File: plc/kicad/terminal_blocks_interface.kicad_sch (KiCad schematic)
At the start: 78 parts, among them CN1 DB128V-5.08-2P-GN-S, CN10 DB128V-5.08-6P-GN-S, CN2 DB128V-5.08-2P-GN-S, CN3 DB128V-5.08-2P-GN-S, CN4 DB128V-5.08-2P-GN-S, CN5 DB128V-5.08-2P-GN-S, CN6 DB128V-5.08-2P-GN-S, CN7 DB128V-5.08-2P-GN-S, CN8 DB128V-5.08-2P-GN-S, CN9 DB128V-5.08-2P-GN-S, Q1 AO3400A, Q2 AO3400A, U1 TCA9535PWR, U2 TPS272C45DRHFR, U3 TPS272C45DRHFR, U4 ADS1115IDGSR, U5 LTV-814S-TA1-A, U6 LTV-814S-TA1-A, U7 LTV-814S-TA1-A, U8 LTV-814S-TA1-A

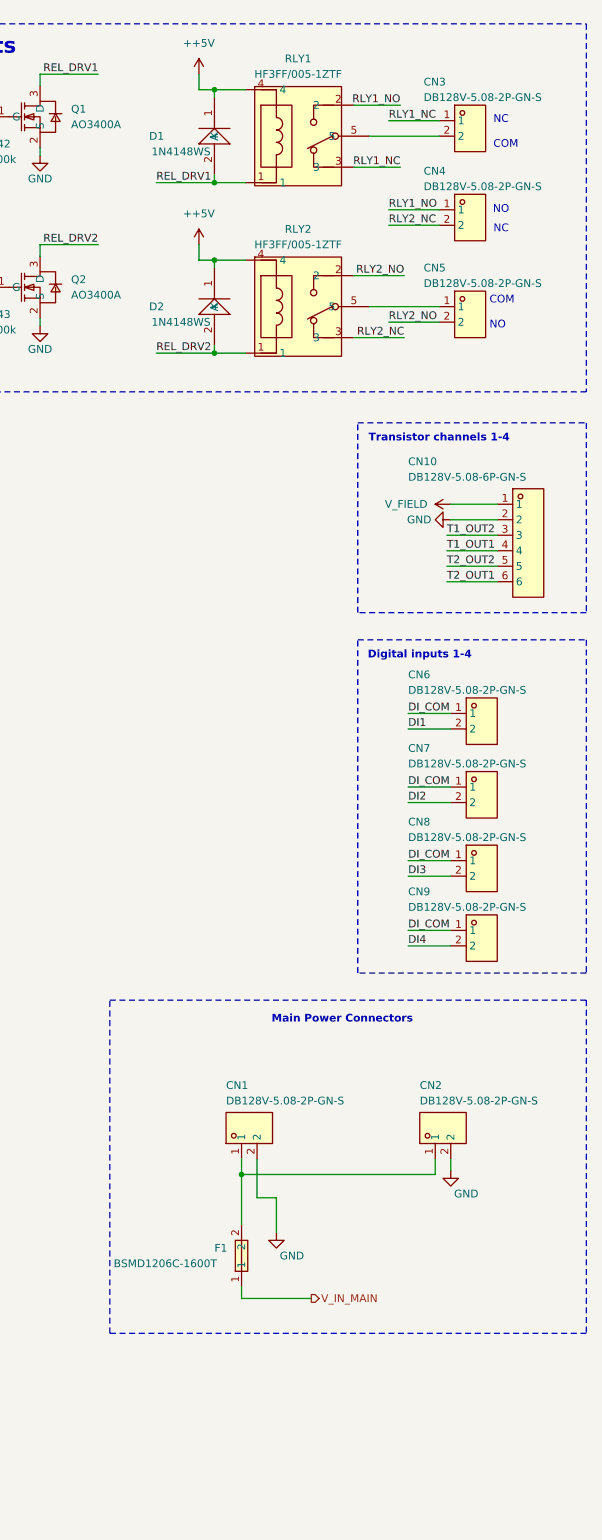
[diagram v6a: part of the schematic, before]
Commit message: Updated PCB placement
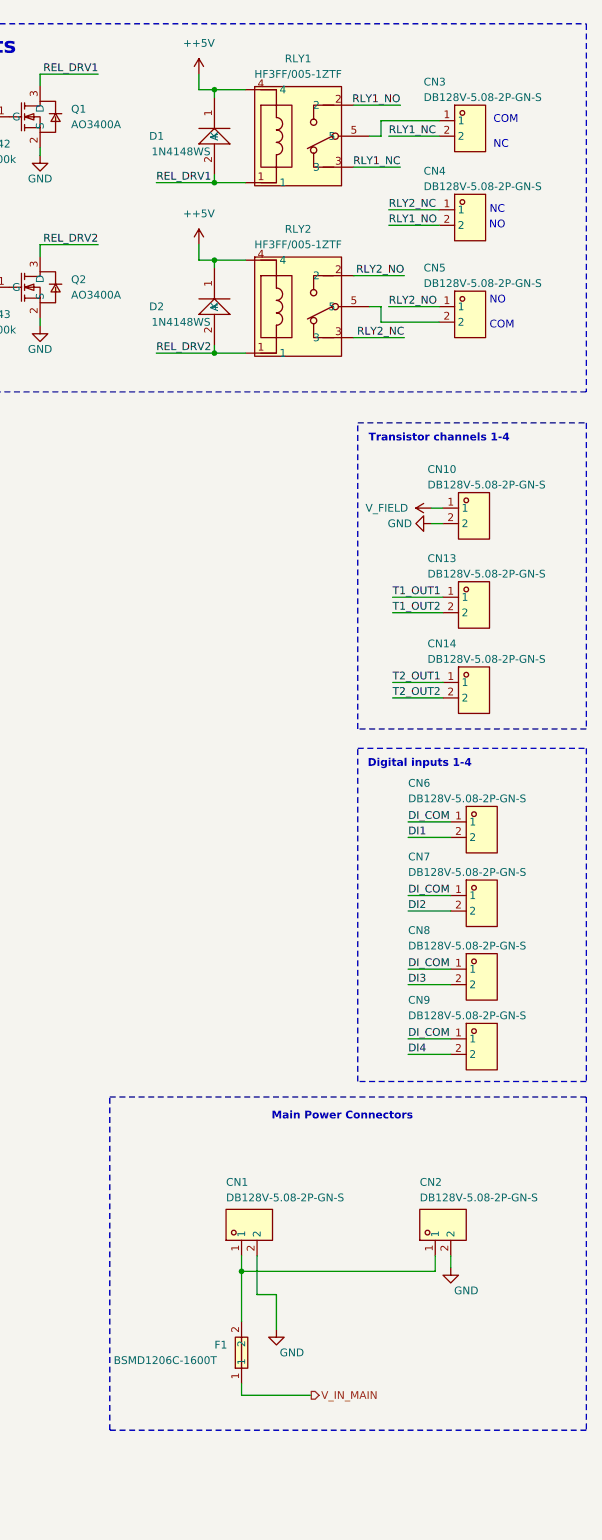
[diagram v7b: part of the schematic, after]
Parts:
- removed CN10: DB128V-5.08-6P-GN-S, LibrePLC32:CONN-TH_6P-P5.08_DIBO_DB128V-5.08, symbol LibrePLC32:DB128V-5.08-6P-GN-S
- added CN10, CN13, CN14: DB128V-5.08-2P-GN-S, LibrePLC32:CONN-TH_2P-P5.08_DIBO_DB128V-5.08, symbol LibrePLC32:DB128V-5.08-2P-GN-S
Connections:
- net GND: now also CN10.2
- net RLY1_NC: now also CN3.2; no longer CN3.1
- net RLY1_NO: now also CN4.2; no longer CN4.1
- net RLY2_NC: now also CN4.1; no longer CN4.2
- net RLY2_NO: now also CN5.1; no longer CN5.2
- net T1_OUT1: now also CN13.1
- net T1_OUT2: now also CN13.2
- net T2_OUT1: now also CN14.1
- net T2_OUT2: now also CN14.2
- net V_FIELD: now also CN10.1
- net at RLY1.5: now also CN3.1; no longer CN3.2
- net at RLY2.5: now also CN5.2; no longer CN5.1
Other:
- note added: "COM NC"
- note added: "NO COM"
- note removed: "COM NO"
- note removed: "NC COM"
- moved on the sheet: CN1, CN2, CN6, CN7, CN8, CN9, F1

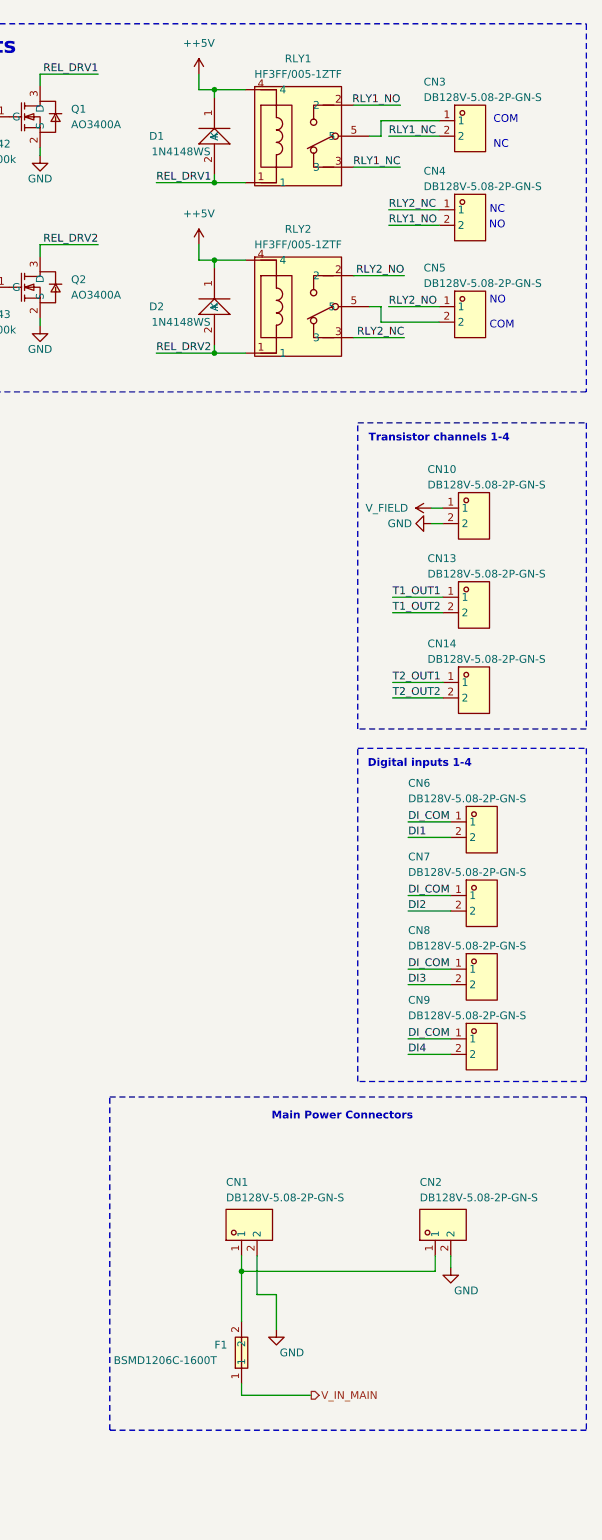
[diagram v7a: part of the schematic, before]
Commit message: Added mounting holes & PCB outline
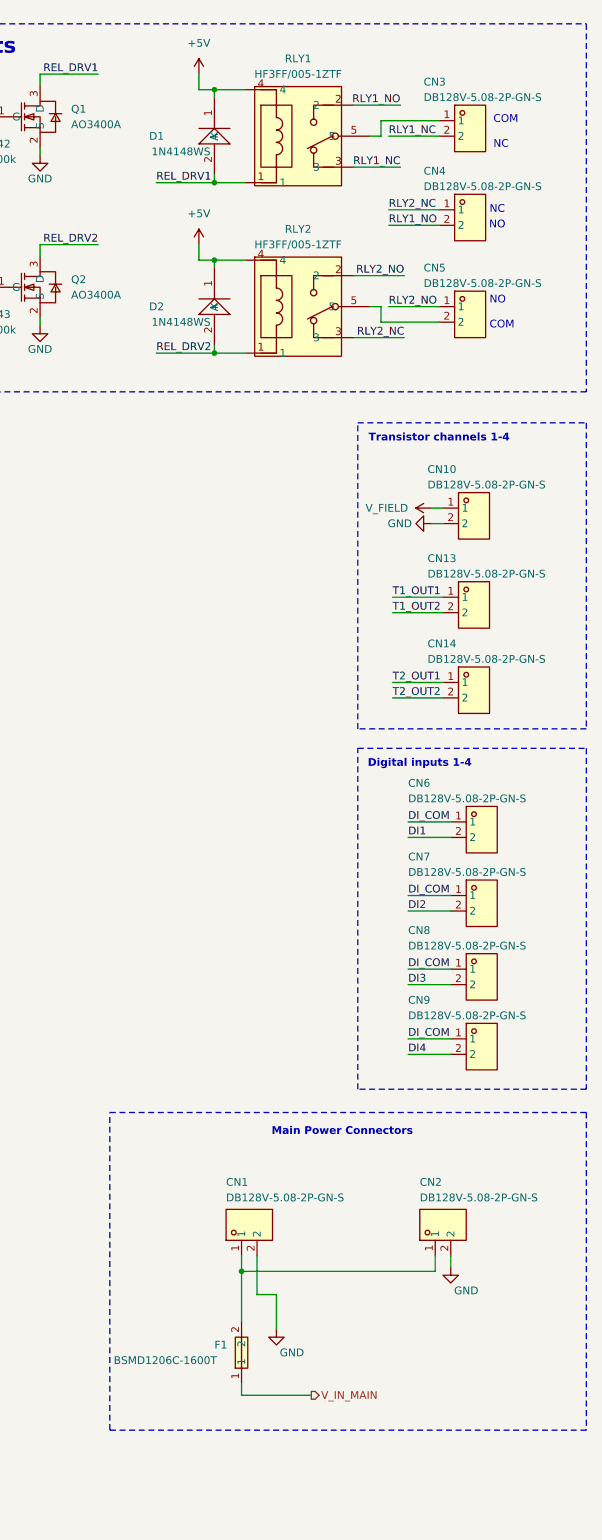
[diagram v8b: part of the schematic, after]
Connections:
- net ++5V renamed +5V
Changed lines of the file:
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@@
 	(rectangle
 		(start 361.95 137.795)
-		(end 399.415 192.405)
+		(end 399.415 193.675)
 		(stroke
 			(width 0)
@@
 	)
 	(rectangle
-		(start 321.31 194.945)
+		(start 321.31 197.485)
 		(end 399.415 249.555)
 		(stroke
@@
 	(text "Main Power Connectors"
 		(exclude_from_sim no)
-		(at 359.41 198.12 0)
+		(at 359.41 200.66 0)
 		(effects
 			(font
@@
 			)
 		)
-		(property "Value" "++5V"
+		(property "Value" "+5V"
 			(at 335.915 50.165 0)
 			(show_name no)
@@
 			)
 		)
-		(property "Value" "++5V"
+		(property "Value" "+5V"
 			(at 335.915 22.225 0)
 			(show_name no)
